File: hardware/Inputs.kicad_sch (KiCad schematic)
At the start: 1 part, among them J1 SWD

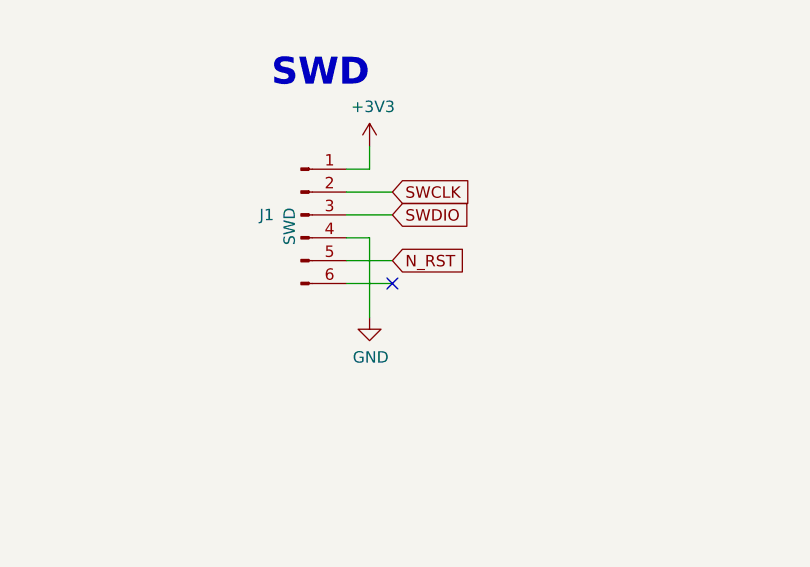
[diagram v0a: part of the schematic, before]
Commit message: added traceswo from pin 55 to progrmator
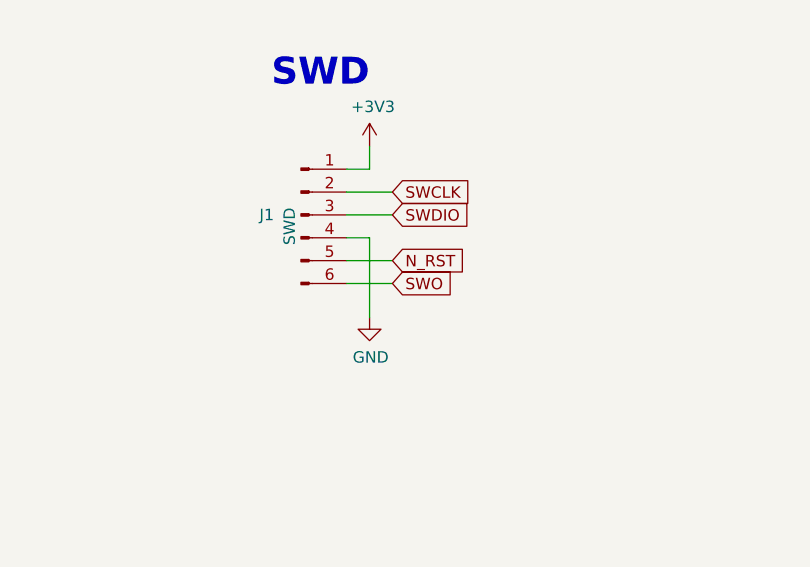
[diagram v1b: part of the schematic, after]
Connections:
- net SWO: now reaches J1.6 (Pin_6)
- no-connect marks 1 -> 0
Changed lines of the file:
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@@
 (kicad_sch (version 20211123) (generator eeschema)
   (paper "A4")
-  (no_connect (at 236.474 136.398))
   (wire (pts (xy 236.474 128.778) (xy 231.394 128.778))
     (stroke (width 0) (type default) (color 0 0 0 0))
@@
     (stroke (width 0) (type default) (color 0 0 0 0))
   )
-  (wire (pts (xy 236.474 136.398) (xy 231.394 136.398))
+  (wire (pts (xy 231.394 136.398) (xy 236.474 136.398))
     (stroke (width 0) (type default) (color 0 0 0 0))
   )
@@
     )
   )
+  (global_label "SWO" (shape input) (at 236.474 136.398 0) (fields_autoplaced)
+    (effects (font (size 1.27 1.27)) (justify left))
+    (property "Intersheet References" "${INTERSHEET_REFS}" (id 0) (at 242.7896 136.3186 0)
+      (effects (font (size 1.27 1.27)) (justify left) hide)
+    )
+  )

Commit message: fuck
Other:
- note added: "hv_sense"
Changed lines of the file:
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@@
     (effects (font (size 2.9972 2.9972) (thickness 0.5994) bold) (justify right bottom))
+  )
+  (text "hv_sense" (at 57.15 105.41 0)
+    (effects (font (size 1.27 1.27)) (justify left bottom))
   )
   (text "SWD" (at 233.934 114.808 180)

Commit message: jolo
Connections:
- net GND: now also J1.3 (Pin_3); no longer J1.4 (Pin_4)
- net SWDIO: now also J1.4 (Pin_4); no longer J1.3 (Pin_3)
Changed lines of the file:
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@@
 (kicad_sch (version 20211123) (generator eeschema)
   (paper "A4")
-  (wire (pts (xy 236.474 128.778) (xy 231.394 128.778))
+  (wire (pts (xy 236.474 131.318) (xy 231.394 131.318))
     (stroke (width 0) (type default) (color 0 0 0 0))
   )
@@
   )
   (wire (pts (xy 241.046 64.77) (xy 238.506 64.77))
+    (stroke (width 0) (type default) (color 0 0 0 0))
+  )
+  (wire (pts (xy 233.934 128.778) (xy 233.934 140.208))
     (stroke (width 0) (type default) (color 0 0 0 0))
   )
@@
   )
   (wire (pts (xy 124.46 74.676) (xy 118.11 74.676))
-    (stroke (width 0) (type default) (color 0 0 0 0))
-  )
-  (wire (pts (xy 233.934 131.318) (xy 231.394 131.318))
     (stroke (width 0) (type default) (color 0 0 0 0))
   )
@@
     (stroke (width 0) (type default) (color 0 0 0 0))
   )
+  (wire (pts (xy 231.394 128.778) (xy 233.934 128.778))
+    (stroke (width 0) (type default) (color 0 0 0 0))
+  )
   (wire (pts (xy 123.698 113.284) (xy 117.348 113.284))
     (stroke (width 0) (type default) (color 0 0 0 0))
@@
   )
   (wire (pts (xy 42.672 113.03) (xy 49.022 113.03))
-    (stroke (width 0) (type default) (color 0 0 0 0))
-  )
-  (wire (pts (xy 233.934 131.318) (xy 233.934 140.208))
     (stroke (width 0) (type default) (color 0 0 0 0))
   )
@@
     )
   )
-  (global_label "SWDIO" (shape input) (at 236.474 128.778 0) (fields_autoplaced)
+  (global_label "SWDIO" (shape input) (at 236.474 131.318 0) (fields_autoplaced)
     (effects (font (size 1.27 1.27)) (justify left))
-    (property "Intersheet References" "${INTERSHEET_REFS}" (id 0) (at -267.716 -156.972 0)
+    (property "Intersheet References" "${INTERSHEET_REFS}" (id 0) (at -267.716 -154.432 0)
       (effects (font (size 1.27 1.27)) hide)
     )

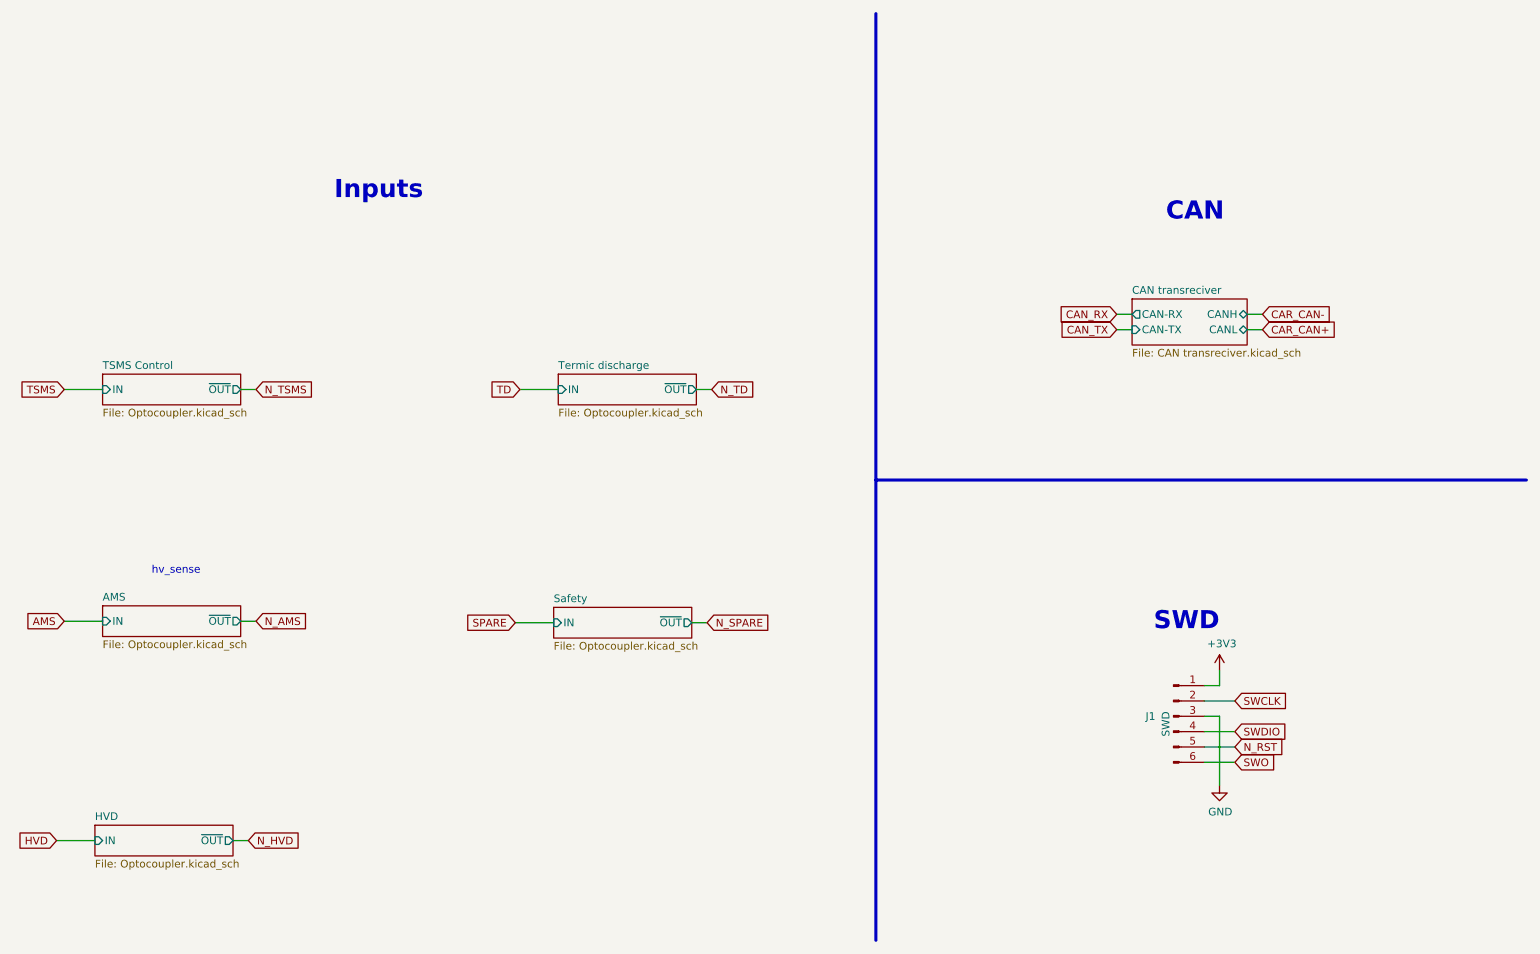
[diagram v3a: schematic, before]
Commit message: major schematic update, changed optocouplers for different, added new fuses for 5v supply for water and potentiometers and 24v supply for BSPD/ESB, updated autosport connector, and some other changes
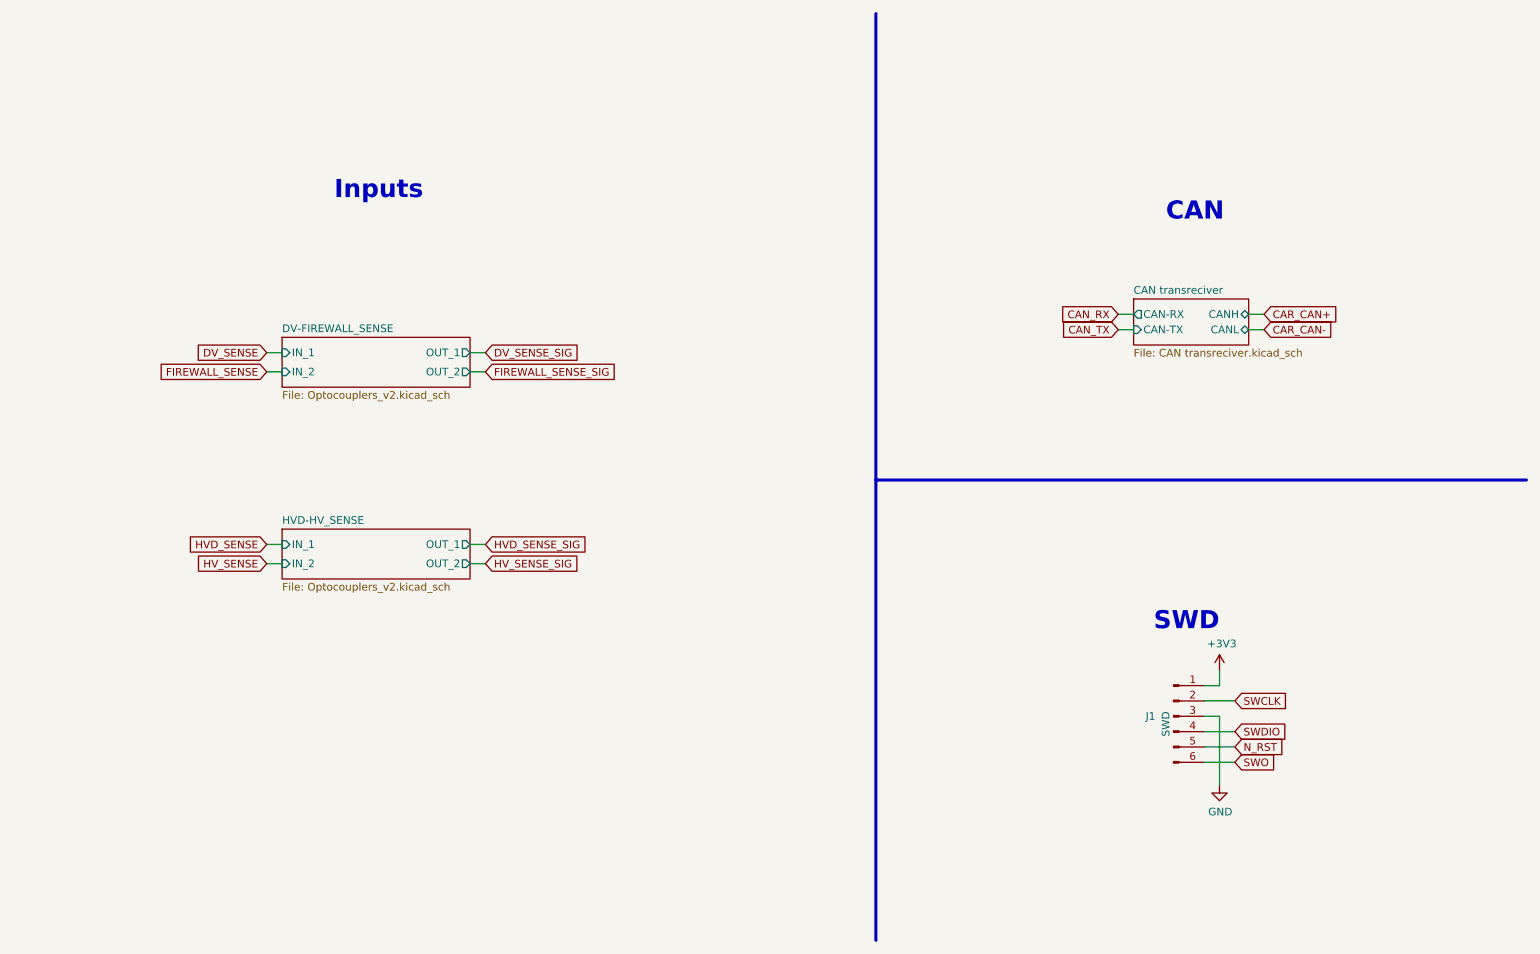
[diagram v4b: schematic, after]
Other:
- removed sheet AMS
- removed sheet HVD
- removed sheet Safety
- removed sheet TSMS Control
- removed sheet Termic discharge
- added sheet DV-FIREWALL_SENSE (Optocouplers_v2.kicad_sch)
- added sheet HVD-HV_SENSE (Optocouplers_v2.kicad_sch)
- note removed: "hv_sense"

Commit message: changed some footprints for clarity, and made some progress on board
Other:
- added sheet INVERTER-SPARE_1 (Optocouplers_v2.kicad_sch)
- added sheet SPARE_2-3 (Optocouplers_v2.kicad_sch)

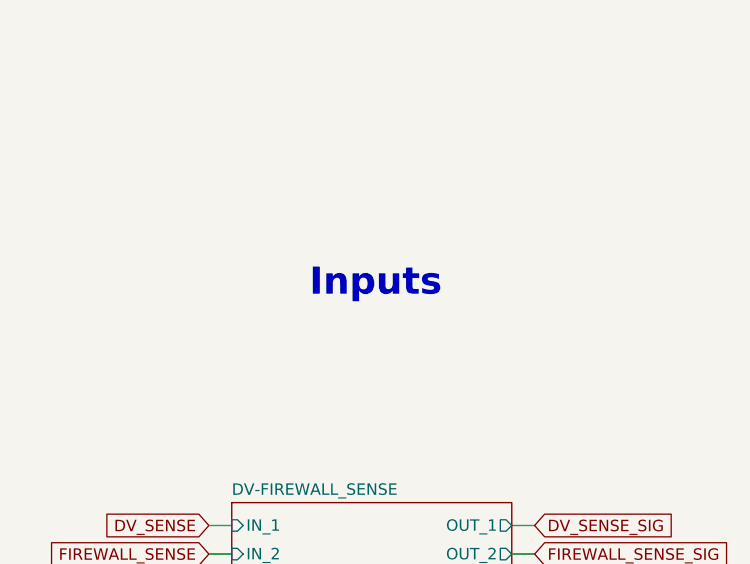
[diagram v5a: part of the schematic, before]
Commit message: debuged the board, changed one opto for mosfet, changed the way water and potentiometers were supplied. Also standrised opamps (yoinked opamps from data Data_Acquisition_Cards)
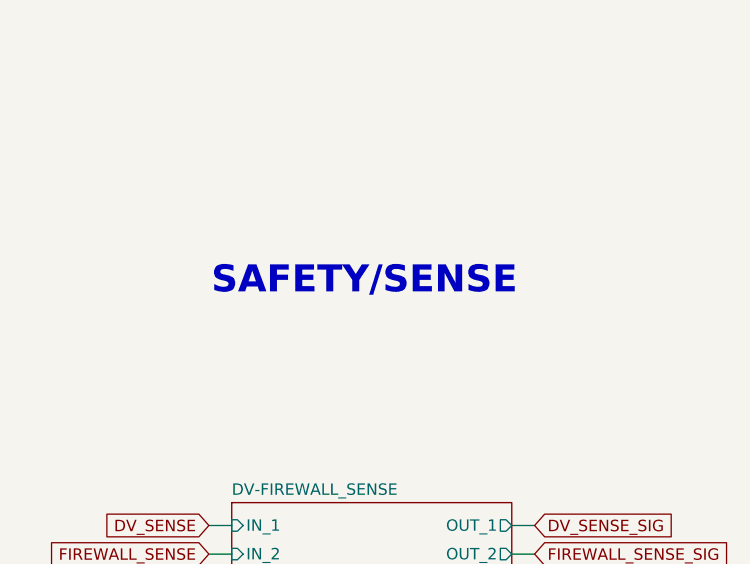
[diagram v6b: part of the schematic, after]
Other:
- note added: "SAFETY/SENSE"
- note removed: "Inputs"
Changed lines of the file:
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@@
     (stroke (width 0) (type default) (color 0 0 0 0))
   )
-  (text "Inputs" (at 102.108 43.434 180)
+  (text "SAFETY/SENSE" (at 110.49 43.18 180)
     (effects (font (size 2.9972 2.9972) (thickness 0.5994) bold) (justify right bottom))
   )
